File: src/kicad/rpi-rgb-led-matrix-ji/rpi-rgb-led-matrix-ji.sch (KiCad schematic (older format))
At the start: 42 parts, among them J1 Conn_01x02_Male, J2 Conn_02x10_Odd_Even, J3 Screw_Terminal_01x02, J4 Conn_02x08_Odd_Even, J5 Conn_02x08_Odd_Even, J6 Conn_02x08_Odd_Even, P1 Raspberry_Pi_2_3, Q1 DMG2305UX, Q2 DMMT5401, U1 74HCT245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

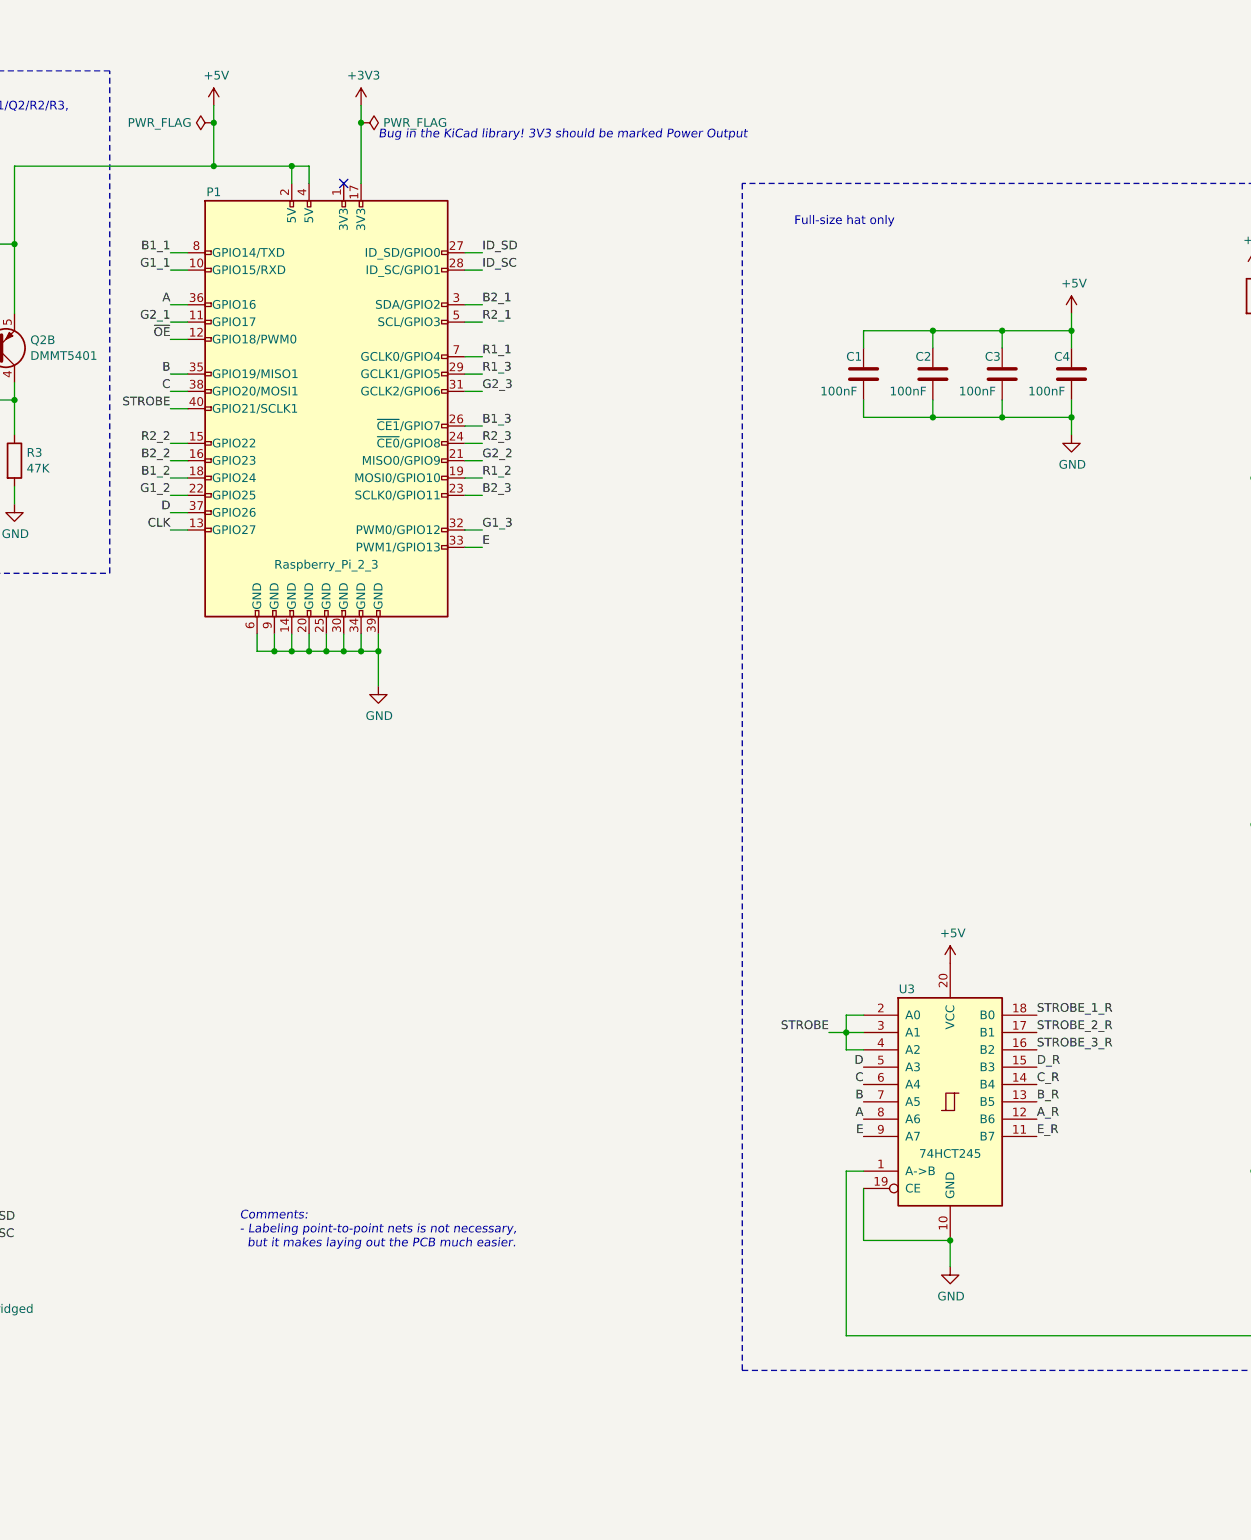
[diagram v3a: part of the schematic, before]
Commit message: rerouted to expose control signals on optional headers
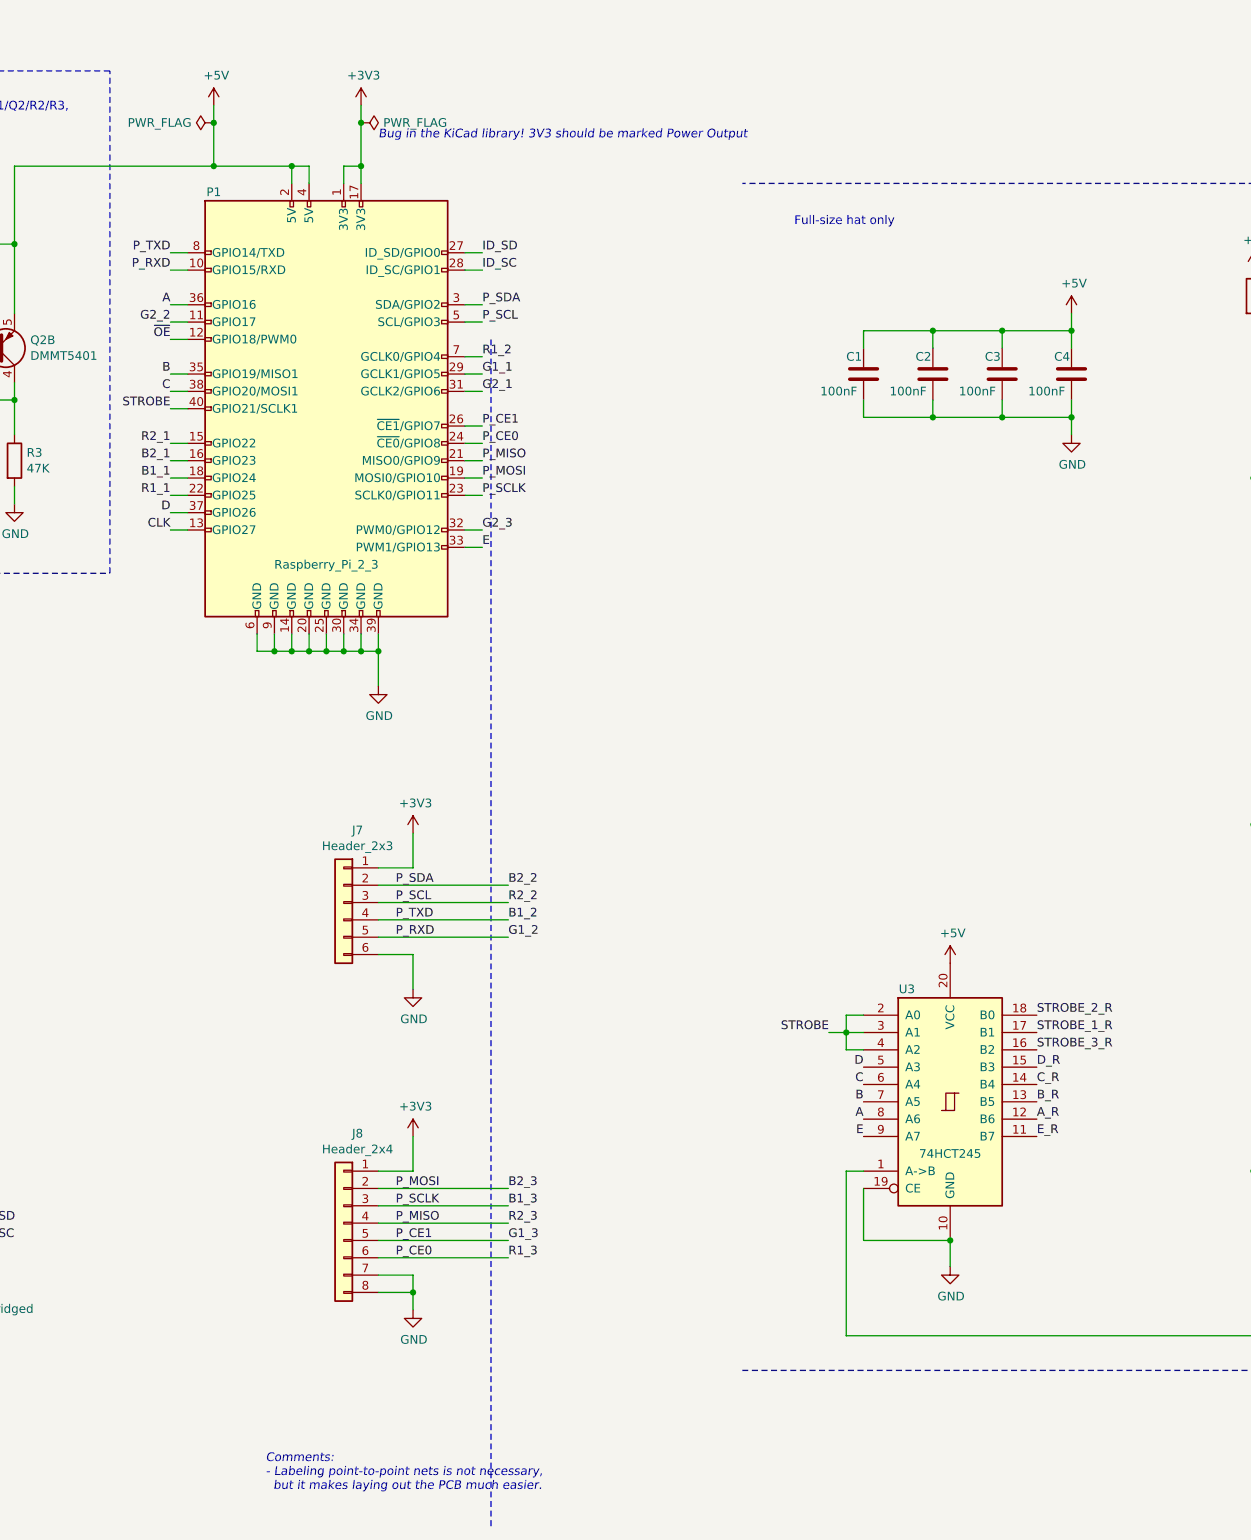
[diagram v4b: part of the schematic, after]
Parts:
- added J7: Header_2x3, Connector_PinHeader_2.54mm:PinHeader_2x03_P2.54mm_Vertical, symbol Connector_Generic:Conn_01x06
- added J8: Header_2x4, Connector_PinHeader_2.54mm:PinHeader_2x04_P2.54mm_Vertical, symbol Connector_Generic:Conn_01x08
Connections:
- net +3V3: now also P1.1 (3V3), J7.1 (Pin_1), J8.1 (Pin_1)
- net B1_1: now also P1.18 (GPIO24); no longer P1.8 (GPIO14/TXD)
- net B1_2: now also P1.8 (GPIO14/TXD), J7.4 (Pin_4); no longer P1.18 (GPIO24)
- net B1_3: now also P1.23 (SCLK0/GPIO11), J8.3 (Pin_3); no longer P1.26 (~CE1~/GPIO7)
- net B2_1: now also P1.16 (GPIO23); no longer P1.3 (SDA/GPIO2)
- net B2_2: now also P1.3 (SDA/GPIO2), J7.2 (Pin_2); no longer P1.16 (GPIO23)
- net B2_3: now also P1.19 (MOSI0/GPIO10), J8.2 (Pin_2); no longer P1.23 (SCLK0/GPIO11)
- net G1_1: now also P1.29 (GCLK1/GPIO5); no longer P1.10 (GPIO15/RXD)
- net G1_2: now also P1.10 (GPIO15/RXD), J7.5 (Pin_5); no longer P1.22 (GPIO25)
- net G1_3: now also P1.26 (~CE1~/GPIO7), J8.5 (Pin_5); no longer P1.32 (PWM0/GPIO12)
- net G2_1: now also P1.31 (GCLK2/GPIO6); no longer P1.11 (GPIO17)
- net G2_2: now also P1.11 (GPIO17); no longer P1.21 (MISO0/GPIO9)
- net G2_3: now also P1.32 (PWM0/GPIO12); no longer P1.31 (GCLK2/GPIO6)
- net GND: now also J7.6 (Pin_6), J8.7 (Pin_7), J8.8 (Pin_8)
- net R1_1: now also P1.22 (GPIO25); no longer P1.7 (GCLK0/GPIO4)
- net R1_2: now also P1.7 (GCLK0/GPIO4); no longer P1.19 (MOSI0/GPIO10)
- net R2_1: now also P1.15 (GPIO22); no longer P1.5 (SCL/GPIO3)
- net STROBE_1_R: now also U3.17 (B1); no longer U3.18 (B0)
- net STROBE_2_R: now also U3.18 (B0); no longer U3.17 (B1)
- net R1_3 renamed P_CE0
- net P_CE0: now also P1.24 (~CE0~/GPIO8), J8.6 (Pin_6); no longer P1.29 (GCLK1/GPIO5)
- net R2_2 renamed P_SCL
- net P_SCL: now also P1.5 (SCL/GPIO3), J7.3 (Pin_3); no longer P1.15 (GPIO22)
- net R2_3 renamed P_MISO
- net P_MISO: now also P1.21 (MISO0/GPIO9), J8.4 (Pin_4); no longer P1.24 (~CE0~/GPIO8)
- no-connect marks 5 -> 4
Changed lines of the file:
@@
 Sheet 1 1
 Title "Led matrix driver"
-Date "2019-03-27"
-Rev "1.2.4"
+Date "2019-03-29"
+Rev "2.0.1"
 Comp "TLA CONSULTING, LLC"
 Comment1 ""
@@
 	1    0    0    -1
 $EndComp
-Text Label 6350 4050 0    50   ~ 0
+Text Label 4550 4850 2    50   ~ 0
 R1_1
-Text Label 4550 3550 2    50   ~ 0
+Text Label 6350 4150 0    50   ~ 0
 G1_1
-Text Label 4550 3450 2    50   ~ 0
+Text Label 4550 4750 2    50   ~ 0
 B1_1
-Text Label 4550 3850 2    50   ~ 0
+Text Label 6350 4250 0    50   ~ 0
 G2_1
 Text Label 4550 4350 2    50   ~ 0
@@
 Wire Wire Line
 	4650 3550 4550 3550
-Text Label 6350 3750 0    50   ~ 0
+Text Label 4550 4650 2    50   ~ 0
 B2_1
-Text Label 6350 3850 0    50   ~ 0
+Text Label 4550 4550 2    50   ~ 0
 R2_1
 NoConn ~ 13850 2350
@@
 Text Label 6350 5150 0    50   ~ 0
 E
-Text Label 4550 4850 2    50   ~ 0
+Text Label 6500 7400 0    50   ~ 0
 G1_2
-Text Label 6350 4650 0    50   ~ 0
+Text Label 4550 3850 2    50   ~ 0
 G2_2
-Text Label 6350 4750 0    50   ~ 0
+Text Label 6350 4050 0    50   ~ 0
 R1_2
-Text Label 4550 4750 2    50   ~ 0
+Text Label 6500 7300 0    50   ~ 0
 B1_2
-Text Label 4550 4550 2    50   ~ 0
+Text Label 6500 7200 0    50   ~ 0
 R2_2
-Text Label 4550 4650 2    50   ~ 0
+Text Label 6500 7100 0    50   ~ 0
 B2_2
+Text Label 6500 9150 0    50   ~ 0
+G1_3
 Text Label 6350 5050 0    50   ~ 0
-G1_3
-Text Label 6350 4250 0    50   ~ 0
 G2_3
-Text Label 6350 4150 0    50   ~ 0
+Text Label 6500 9250 0    50   ~ 0
 R1_3
-Text Label 6350 4450 0    50   ~ 0
+Text Label 6500 8950 0    50   ~ 0
 B1_3
-Text Label 6350 4550 0    50   ~ 0
+Text Label 6500 9050 0    50   ~ 0
 R2_3
-Text Label 6350 4850 0    50   ~ 0
+Text Label 6500 8850 0    50   ~ 0
 B2_3
 Wire Wire Line
@@
 	15350 3050 7850 3050
 Wire Notes Line
-	7850 3050 7850 9900
+	6400 3950 6400 10800
 Wire Notes Line
 	7850 9900 15350 9900
@@
 Text Label 13950 4650 0    50   ~ 0
 STROBE_1_R
-Text Notes 4950 9200 0    50   Italic 0
+Text Notes 5100 10600 0    50   Italic 0
 Comments:\n- Labeling point-to-point nets is not necessary,\n  but it makes laying out the PCB much easier.
 Text Notes 1600 8150 0    50   ~ 0
@@
 Text Label 11350 8550 2    50   ~ 0
 ~OE
-Text Label 9550 7950 0    50   ~ 0
+Text Label 9550 7850 0    50   ~ 0
 STROBE_2_R
 Text Label 9550 8050 0    50   ~ 0
 STROBE_3_R
-Text Label 9550 7850 0    50   ~ 0
+Text Label 9550 7950 0    50   ~ 0
 STROBE_1_R
 $Comp
@@
 Connection ~ 5650 2700
 Wire Wire Line
-	5650 2700 5650 3050
-NoConn ~ 5550 3050
+	5650 2700 5650 2950
 Wire Wire Line
 	1250 3050 1250 3150
@@
 	1600 8950 1600 9750
 Connection ~ 1850 9750
+Text Label 6350 3750 0    50   ~ 0
+P_SDA
+Text Label 6350 3850 0    50   ~ 0
+P_SCL
+Text Label 6350 4450 0    50   ~ 0
+P_CE1
+Text Label 6350 4550 0    50   ~ 0
+P_CE0
+Text Label 6350 4650 0    50   ~ 0
+P_MISO
+Text Label 6350 4750 0    50   ~ 0
+P_MOSI
+Text Label 6350 4850 0    50   ~ 0
+P_SCLK
+Text Label 4550 3450 2    50   ~ 0
+P_TXD
+Text Label 4550 3550 2    50   ~ 0
+P_RXD
+Text Label 5850 7100 0    50   ~ 0
+P_SDA
+Text Label 5850 7200 0    50   ~ 0
+P_SCL
+Text Label 5850 9150 0    50   ~ 0
+P_CE1
+Text Label 5850 9250 0    50   ~ 0
+P_CE0
+Text Label 5850 9050 0    50   ~ 0
+P_MISO
+Text Label 5850 8850 0    50   ~ 0
+P_MOSI
+Text Label 5850 8950 0    50   ~ 0
+P_SCLK
+Text Label 5850 7300 0    50   ~ 0
+P_TXD
+Text Label 5850 7400 0    50   ~ 0
+P_RXD
+$Comp
+L power:GND #PWR023
+U 1 1 5D41A0EA
+P 5950 7700
+F 0 "#PWR023" H 5950 7450 50  0001 C CNN
+F 1 "GND" H 5955 7527 50  0000 C CNN
+F 2 "" H 5950 7700 50  0001 C CNN
+F 3 "" H 5950 7700 50  0001 C CNN
+	1    5950 7700
+	1    0    0    -1
+$EndComp
+$Comp
+L power:+3V3 #PWR022
+U 1 1 5D4391C5
+P 5950 6800
+F 0 "#PWR022" H 5950 6650 50  0001 C CNN
+F 1 "+3V3" H 5965 6973 50  0000 C CNN
+F 2 "" H 5950 6800 50  0001 C CNN
+F 3 "" H 5950 6800 50  0001 C CNN
+	1    5950 6800
+	1    0    0    -1
+$EndComp
+Wire Wire Line
+	5750 7100 6500 7100
+Wire Wire Line
+	5750 7200 6500 7200
+Wire Wire Line
+	5750 7300 6500 7300
+Wire Wire Line
+	5750 7400 6500 7400
+Wire Wire Line
+	5750 9150 6500 9150
+Wire Wire Line
+	5750 9250 6500 9250
+Wire Wire Line
+	5750 9050 6500 9050
+Wire Wire Line
+	5750 8850 6500 8850
+Wire Wire Line
+	5750 8950 6500 8950
+Wire Wire Line
+	5750 7000 5950 7000
+Wire Wire Line
+	5950 7000 5950 6800
+Wire Wire Line
+	5750 7500 5950 7500
+Wire Wire Line
+	5950 7500 5950 7700
+$Comp
+L power:+3V3 #PWR024
+U 1 1 5D5EFD57
+P 5950 8550
+F 0 "#PWR024" H 5950 8400 50  0001 C CNN
+F 1 "+3V3" H 5965 8723 50  0000 C CNN
+F 2 "" H 5950 8550 50  0001 C CNN
+F 3 "" H 5950 8550 50  0001 C CNN
+	1    5950 8550
+	1    0    0    -1
+$EndComp
+Wire Wire Line
+	5750 8750 5950 8750
+Wire Wire Line
+	5950 8750 5950 8550
+$Comp
+L power:GND #PWR025
+U 1 1 5D62E563
+P 5950 9550
+F 0 "#PWR025" H 5950 9300 50  0001 C CNN
+F 1 "GND" H 5955 9377 50  0000 C CNN
+F 2 "" H 5950 9550 50  0001 C CNN
+F 3 "" H 5950 9550 50  0001 C CNN
+	1    5950 9550
+	1    0    0    -1
+$EndComp
+Wire Wire Line
+	5750 9350 5950 9350
+Wire Wire Line
+	5950 9350 5950 9450
+$Comp
+L Connector_Generic:Conn_01x06 J7
+U 1 1 5D66E386
+P 5550 7200
+F 0 "J7" H 5470 7617 50  0000 C CNN
+F 1 "Header_2x3" H 5470 7526 50  0000 C CNN
+F 2 "Connector_PinHeader_2.54mm:PinHeader_2x03_P2.54mm_Vertical" H 5550 7200 50  0001 C CNN
+F 3 "~" H 5550 7200 50  0001 C CNN
+	1    5550 7200
+	-1   0    0    -1
+$EndComp
+$Comp
+L Connector_Generic:Conn_01x08 J8
+U 1 1 5D66E650
+P 5550 9050
+F 0 "J8" H 5470 9567 50  0000 C CNN
+F 1 "Header_2x4" H 5470 9476 50  0000 C CNN
+F 2 "Connector_PinHeader_2.54mm:PinHeader_2x04_P2.54mm_Vertical" H 5550 9050 50  0001 C CNN
+F 3 "~" H 5550 9050 50  0001 C CNN
+	1    5550 9050
+	-1   0    0    -1
+$EndComp
+Wire Wire Line
+	5750 9450 5950 9450
+Connection ~ 5950 9450
+Wire Wire Line
+	5950 9450 5950 9550
+Wire Wire Line
+	5550 3050 5550 2950
+Wire Wire Line
+	5550 2950 5650 2950
+Connection ~ 5650 2950
+Wire Wire Line
+	5650 2950 5650 3050
 $EndSCHEMATC

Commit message: m
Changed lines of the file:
@@
 	15350 3050 7850 3050
 Wire Notes Line
-	6400 3950 6400 10800
+	7850 3050 7850 9900
 Wire Notes Line
 	7850 9900 15350 9900
